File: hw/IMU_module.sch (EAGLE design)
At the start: 42 parts, among them J1 GROVE-4P-2.0-3470130P1, J2 GROVE-4P-2.0-3470130P1, X1 53047-06

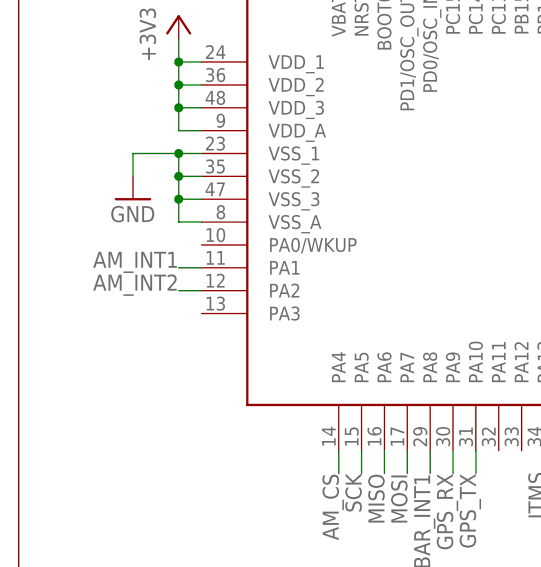
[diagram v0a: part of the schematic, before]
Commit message: moved LSM303D interrupt lines
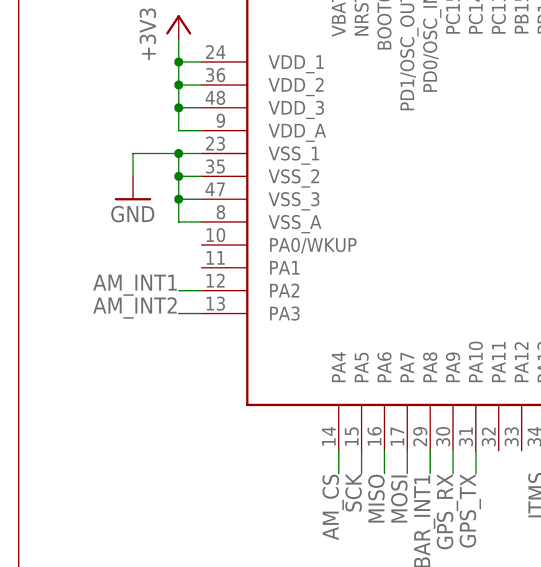
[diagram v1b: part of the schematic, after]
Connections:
- net AM_INT1: now also U$6.PA2; no longer U$6.PA1
- net AM_INT2: now also U$6.PA3; no longer U$6.PA2
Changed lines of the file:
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@@
 <net name="AM_INT1" class="0">
 <segment>
-<pinref part="U$6" gate="G$1" pin="PA1"/>
-<wire x1="25.4" y1="198.12" x2="22.86" y2="198.12" width="0.1524" layer="91"/>
-<label x="22.86" y="198.12" size="1.778" layer="95" rot="MR0"/>
+<wire x1="25.4" y1="195.58" x2="22.86" y2="195.58" width="0.1524" layer="91"/>
+<label x="22.86" y="195.58" size="1.778" layer="95" rot="MR0"/>
+<pinref part="U$6" gate="G$1" pin="PA2"/>
 </segment>
 <segment>
@@
 <net name="AM_INT2" class="0">
 <segment>
-<pinref part="U$6" gate="G$1" pin="PA2"/>
-<wire x1="25.4" y1="195.58" x2="22.86" y2="195.58" width="0.1524" layer="91"/>
-<label x="22.86" y="195.58" size="1.778" layer="95" rot="MR0"/>
+<wire x1="25.4" y1="193.04" x2="22.86" y2="193.04" width="0.1524" layer="91"/>
+<label x="22.86" y="193.04" size="1.778" layer="95" rot="MR0"/>
+<pinref part="U$6" gate="G$1" pin="PA3"/>
 </segment>
 <segment>

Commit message: approved DRC false errors
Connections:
- net BAR_CS: now also U$9.CS; no longer U$9.SCL/SPC
- net MISO: now also U$9.SDO; no longer U$9.CS
- net MOSI: now also U$9.SDA/SDI; no longer U$9.SDO
- net SCK: now also U$9.SCL/SPC; no longer U$9.SDA/SDI
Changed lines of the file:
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@@
-</segment>
-<segment>
-<wire x1="172.72" y1="111.76" x2="170.18" y2="111.76" width="0.1524" layer="91"/>
-<label x="160.02" y="111.76" size="1.778" layer="95"/>
-<pinref part="U$9" gate="G$1" pin="SDA/SDI"/>
 </segment>
 <segment>
@@
 <label x="43.18" y="175.26" size="1.778" layer="95" rot="MR270"/>
 </segment>
+<segment>
+<wire x1="172.72" y1="114.3" x2="167.64" y2="114.3" width="0.1524" layer="91"/>
+<label x="160.02" y="114.3" size="1.778" layer="95"/>
+<pinref part="U$9" gate="G$1" pin="SCL/SPC"/>
+</segment>
 </net>
 <net name="MISO" class="0">
@@
 <label x="172.72" y="236.22" size="1.778" layer="95" rot="MR0"/>
 <pinref part="U$7" gate="G$1" pin="SDO"/>
-</segment>
-<segment>
-<wire x1="172.72" y1="106.68" x2="170.18" y2="106.68" width="0.1524" layer="91"/>
-<label x="160.02" y="106.68" size="1.778" layer="95"/>
-<pinref part="U$9" gate="G$1" pin="CS"/>
 </segment>
 <segment>
@@
 <label x="45.72" y="175.26" size="1.778" layer="95" rot="MR270"/>
 </segment>
+<segment>
+<wire x1="172.72" y1="109.22" x2="167.64" y2="109.22" width="0.1524" layer="91"/>
+<label x="160.02" y="109.22" size="1.778" layer="95"/>
+<pinref part="U$9" gate="G$1" pin="SDO"/>
+</segment>
 </net>
 <net name="MOSI" class="0">
@@
 <label x="172.72" y="238.76" size="1.778" layer="95" rot="MR0"/>
 <pinref part="U$7" gate="G$1" pin="SDA/SDI"/>
-</segment>
-<segment>
-<wire x1="172.72" y1="109.22" x2="170.18" y2="109.22" width="0.1524" layer="91"/>
-<label x="160.02" y="109.22" size="1.778" layer="95"/>
-<pinref part="U$9" gate="G$1" pin="SDO"/>
 </segment>
 <segment>
@@
 <wire x1="48.26" y1="177.8" x2="48.26" y2="175.26" width="0.1524" layer="91"/>
 <label x="48.26" y="175.26" size="1.778" layer="95" rot="MR270"/>
+</segment>
+<segment>
+<wire x1="172.72" y1="111.76" x2="167.64" y2="111.76" width="0.1524" layer="91"/>
+<label x="160.02" y="111.76" size="1.778" layer="95"/>
+<pinref part="U$9" gate="G$1" pin="SDA/SDI"/>
 </segment>
 </net>
@@
 <net name="BAR_CS" class="0">
 <segment>
-<wire x1="172.72" y1="114.3" x2="170.18" y2="114.3" width="0.1524" layer="91"/>
-<label x="160.02" y="114.3" size="1.778" layer="95"/>
-<pinref part="U$9" gate="G$1" pin="SCL/SPC"/>
-</segment>
-<segment>
 <pinref part="U$6" gate="G$1" pin="PB12"/>
 <wire x1="68.58" y1="236.22" x2="68.58" y2="238.76" width="0.1524" layer="91"/>
 <label x="68.58" y="238.76" size="1.778" layer="95" rot="R90"/>
 </segment>
+<segment>
+<wire x1="172.72" y1="106.68" x2="167.64" y2="106.68" width="0.1524" layer="91"/>
+<label x="160.02" y="106.68" size="1.778" layer="95"/>
+<pinref part="U$9" gate="G$1" pin="CS"/>
+</segment>
 </net>
